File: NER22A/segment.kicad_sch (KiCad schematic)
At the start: 0 parts

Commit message: Tractive system schematic
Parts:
- added BT? (x80): 18650, symbol Device:Battery_Cell
- added F? (x80): Fuse_Small, symbol Device:Fuse_Small
- added U?: Shepherd_Segment, symbol NER:Shepherd_Segment
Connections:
- new net: BT?.1 (+), F?.1 (x80)
- new net: BT?.2 (-), BT?.2 (-), BT?.2 (-), BT?.2 (-), F?.2, F?.2, F?.2, F?.2 (x19)
- new net GLV_IN: U?. (isoIP_OUT)
- new net GLV_OUT: U?. (isoIP_OUT)
- new net GND_IN: U?. (isoIP_OUT)
- new net GND_OUT: U?. (isoIP_OUT)
- new net Seg+: F?.2, F?.2, F?.2, F?.2
- new net Seg-: BT?.2 (-), BT?.2 (-), BT?.2 (-), BT?.2 (-)
- new net isoIM_IN: U?. (isoIP_OUT)
- new net isoIM_OUT: U?. (isoIP_OUT)
- new net isoIP_IN: U?. (isoIP_OUT)
- new net isoIP_OUT: U?. (isoIP_OUT)

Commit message: Changed some pin names
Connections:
- net GLV_IN is gone; now on net isoIP_OUT: U?. (isoIP_OUT)
- net GLV_OUT is gone; now on net isoIP_OUT: U?. (isoIP_OUT)
- new net 12V_IN: U?. (isoIP_OUT)
- new net 12V_OUT: U?. (isoIP_OUT)
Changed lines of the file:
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@@
     (stroke (width 0) (type default) (color 0 0 0 0))
   )
-  (hierarchical_label "GLV_IN" (shape input) (at 186.69 172.72 180)
+  (hierarchical_label "12V_IN" (shape input) (at 186.69 172.72 180)
     (effects (font (size 1.27 1.27)) (justify right))
   )
@@
     (effects (font (size 1.27 1.27)) (justify left))
   )
-  (hierarchical_label "GLV_OUT" (shape input) (at 247.65 172.72 0)
+  (hierarchical_label "12V_OUT" (shape input) (at 247.65 172.72 0)
     (effects (font (size 1.27 1.27)) (justify left))
   )

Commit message: Changed
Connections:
- net 12V_IN is gone; now on net isoIP_IN: U?. (isoIP_OUT)
- net 12V_OUT is gone; now on net isoIP_IN: U?. (isoIP_OUT)
- net GND_IN is gone; now on net isoIP_IN: U?. (isoIP_OUT)
- net GND_OUT is gone; now on net isoIP_IN: U?. (isoIP_OUT)
- net isoIP_OUT is gone; now on net isoIP_IN: U?. (isoIP_OUT)
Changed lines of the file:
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@@
+    (stroke (width 0) (type default) (color 0 0 0 0))
+  )
+  (wire (pts (xy 247.65 175.26) (xy 247.65 177.8))
     (stroke (width 0) (type default) (color 0 0 0 0))
   )
@@
     (stroke (width 0) (type default) (color 0 0 0 0))
   )
-  (hierarchical_label "12V_IN" (shape input) (at 186.69 172.72 180)
-    (effects (font (size 1.27 1.27)) (justify right))
-  )
-  (hierarchical_label "isoIP_OUT" (shape input) (at 247.65 177.8 0)
+  (hierarchical_label "isoIP_OUT" (shape input) (at 247.65 175.26 0)
     (effects (font (size 1.27 1.27)) (justify left))
   )
-  (hierarchical_label "isoIM_OUT" (shape input) (at 247.65 180.34 0)
-    (effects (font (size 1.27 1.27)) (justify left))
-  )
-  (hierarchical_label "12V_OUT" (shape input) (at 247.65 172.72 0)
-    (effects (font (size 1.27 1.27)) (justify left))
-  )
-  (hierarchical_label "GND_OUT" (shape input) (at 247.65 175.26 0)
+  (hierarchical_label "isoIM_OUT" (shape input) (at 247.65 177.8 0)
     (effects (font (size 1.27 1.27)) (justify left))
   )
@@
     (effects (font (size 1.27 1.27)) (justify left))
   )
-  (hierarchical_label "isoIP_IN" (shape input) (at 186.69 177.8 180)
+  (hierarchical_label "isoIP_IN" (shape input) (at 186.69 175.26 180)
     (effects (font (size 1.27 1.27)) (justify right))
   )
-  (hierarchical_label "isoIM_IN" (shape input) (at 186.69 180.34 180)
-    (effects (font (size 1.27 1.27)) (justify right))
-  )
-  (hierarchical_label "GND_IN" (shape input) (at 186.69 175.26 180)
+  (hierarchical_label "isoIM_IN" (shape input) (at 186.69 177.8 180)
     (effects (font (size 1.27 1.27)) (justify right))
   )
@@
     (pin "")
     (pin "")
-    (pin "")
-    (pin "")
-    (pin "")
-    (pin "")

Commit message: Made some changes
POg
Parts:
- added BT? (x20): 18650, symbol Device:Battery_Cell
- added F? (x20): Fuse_Small, symbol Device:Fuse_Small
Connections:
- net Seg+: now also F?.2
- net Seg-: now also BT?.2 (-)
- net at BT?.2 (-), BT?.2 (-), BT?.2 (-)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: now also BT?.2 (-), F?.2 (x19)
- new net: BT?.1 (+), F?.1 (x20)

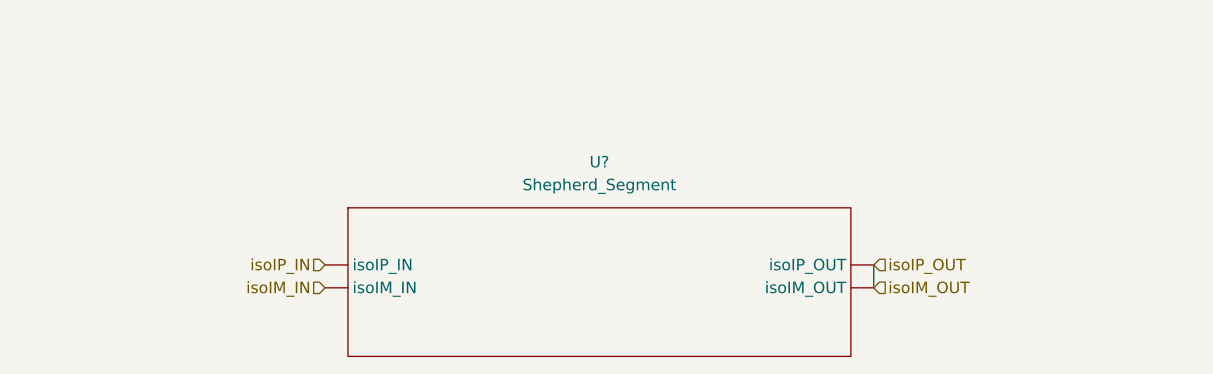
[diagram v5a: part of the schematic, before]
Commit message: Updated wiring
Updated wiring based on wiring table in confluence
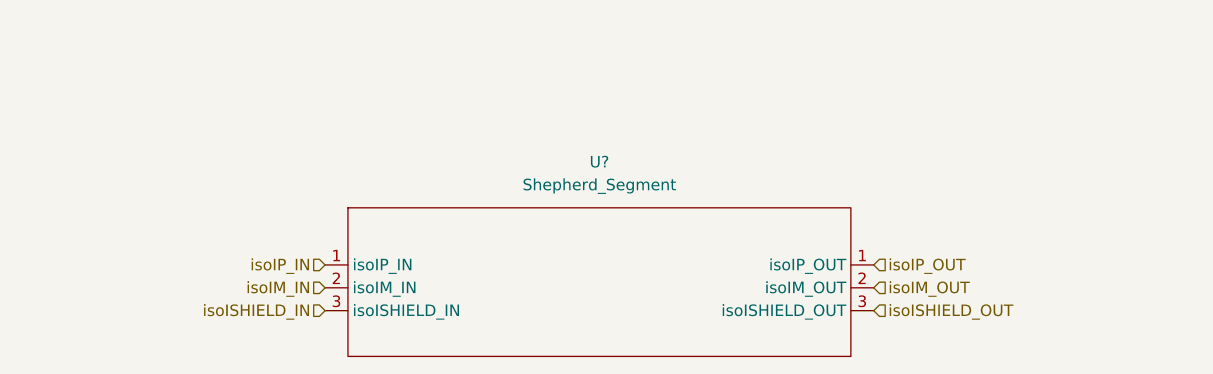
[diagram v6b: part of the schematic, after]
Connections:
- net isoIM_IN: now also U?.2 (isoIM_OUT); no longer U?. (isoIP_OUT)
- net isoIM_OUT: now also U?.2 (isoIM_OUT); no longer U?. (isoIP_OUT)
- net isoIP_IN: now also U?.1 (isoIP_OUT); no longer U?. (isoIP_OUT)
- new net isoIP_OUT: U?.1 (isoIP_OUT)
- new net isoISHIELD_IN: U?.3 (isoISHIELD_OUT)
- new net isoISHIELD_OUT: U?.3 (isoISHIELD_OUT)
